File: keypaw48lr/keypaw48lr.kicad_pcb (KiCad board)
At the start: 2 copper layers, 0 parts

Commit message: feat: layout key matrix with kbplacer
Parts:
- added C1: 10uF, Capacitor_SMD:C_1206_3216Metric_Pad1.33x1.80mm_HandSolder, B.Cu at (97.8, 142.2)
- added C10: 1uF, Capacitor_SMD:C_1206_3216Metric_Pad1.33x1.80mm_HandSolder, B.Cu at (101.6, 150.6)
- added C11: 1uF, Capacitor_SMD:C_1206_3216Metric_Pad1.33x1.80mm_HandSolder, B.Cu at (60.4, 62.4)
- added C2: 100nF, Capacitor_SMD:C_0805_2012Metric_Pad1.18x1.45mm_HandSolder, B.Cu at (93.8, 142.2)
- added C3: 10uF, Capacitor_SMD:C_1206_3216Metric_Pad1.33x1.80mm_HandSolder, B.Cu at (91.2, 150.6)
- added C4: 100nF, Capacitor_SMD:C_0805_2012Metric_Pad1.18x1.45mm_HandSolder, B.Cu at (87.1, 150.6)
- added C5: 4.7uF, Capacitor_SMD:C_1206_3216Metric_Pad1.33x1.80mm_HandSolder, B.Cu at (112.6, 146.4)
- added C6: 100nF, Capacitor_SMD:C_0805_2012Metric_Pad1.18x1.45mm_HandSolder, B.Cu at (113.2, 143.0)
- added C7: 10uF, Capacitor_SMD:C_1206_3216Metric_Pad1.33x1.80mm_HandSolder, B.Cu at (125.2, 147.2)
- added C8: 100nF, Capacitor_SMD:C_0805_2012Metric_Pad1.18x1.45mm_HandSolder, B.Cu at (121.6, 147.2)
- added C9: 1uF, Capacitor_SMD:C_1206_3216Metric_Pad1.33x1.80mm_HandSolder, B.Cu at (111.4, 150.4)
- added D1: D, MX_SW_HS_REV:D_SOD-323_HandSoldering_REV, F.Cu at (83.6, 59.9)
- added D10: D, MX_SW_HS_REV:D_SOD-323_HandSoldering_REV, F.Cu at (140.7, 76.7)
- added D11: D, MX_SW_HS_REV:D_SOD-323_HandSoldering_REV, F.Cu at (159.8, 83.7)
- added D12: D, MX_SW_HS_REV:D_SOD-323_HandSoldering_REV, F.Cu at (178.8, 83.7)
- added D13: D, MX_SW_HS_REV:D_SOD-323_HandSoldering_REV, F.Cu at (83.6, 98.0)
- added D14: D, MX_SW_HS_REV:D_SOD-323_HandSoldering_REV, F.Cu at (102.6, 95.7)
- added D15: D, MX_SW_HS_REV:D_SOD-323_HandSoldering_REV, F.Cu at (121.7, 93.3)
- added D16: D, MX_SW_HS_REV:D_SOD-323_HandSoldering_REV, F.Cu at (140.7, 95.7)
- added D17: D, MX_SW_HS_REV:D_SOD-323_HandSoldering_REV, F.Cu at (159.8, 102.8)
- added D18: D, MX_SW_HS_REV:D_SOD-323_HandSoldering_REV, F.Cu at (178.8, 102.8)
- added D19: D, MX_SW_HS_REV:D_SOD-323_HandSoldering_REV, F.Cu at (76.4, 136.1)
- added D2: D, MX_SW_HS_REV:D_SOD-323_HandSoldering_REV, F.Cu at (102.6, 57.6)
- added D20: D, MX_SW_HS_REV:D_SOD-323_HandSoldering_REV, F.Cu at (64.5, 117.1)
- added D21: D, MX_SW_HS_REV:D_SOD-323_HandSoldering_REV, F.Cu at (83.6, 117.1)
- added D22: D, MX_SW_HS_REV:D_SOD-323_HandSoldering_REV, F.Cu at (87.2, 115.8)
- added D23: D, MX_SW_HS_REV:D_SOD-323_HandSoldering_REV, F.Cu at (159.8, 136.1)
- added D24: D, MX_SW_HS_REV:D_SOD-323_HandSoldering_REV, F.Cu at (178.8, 136.1)
- added D3: D, MX_SW_HS_REV:D_SOD-323_HandSoldering_REV, F.Cu at (121.7, 55.2)
- added D4: D, MX_SW_HS_REV:D_SOD-323_HandSoldering_REV, F.Cu at (140.7, 57.6)
- added D5: D, MX_SW_HS_REV:D_SOD-323_HandSoldering_REV, F.Cu at (159.8, 64.7)
- added D6: D, MX_SW_HS_REV:D_SOD-323_HandSoldering_REV, F.Cu at (178.8, 64.7)
- added D7: D, MX_SW_HS_REV:D_SOD-323_HandSoldering_REV, F.Cu at (83.6, 79.0)
- added D8: D, MX_SW_HS_REV:D_SOD-323_HandSoldering_REV, F.Cu at (102.6, 76.7)
- added D9: D, MX_SW_HS_REV:D_SOD-323_HandSoldering_REV, F.Cu at (121.7, 74.2)
- added J1: Conn_01x02, Connector_Molex:Molex_PicoBlade_53048-0210_1x02_P1.25mm_Horizontal, F.Cu at (105.4, 53.2)
- added J2: Conn_01x02, Connector_Molex:Molex_PicoBlade_53048-0210_1x02_P1.25mm_Horizontal, F.Cu at (65.2, 64.3)
- added J3: Conn_01x02, Connector_Molex:Molex_PicoBlade_53048-0210_1x02_P1.25mm_Horizontal, F.Cu at (94.4, 128.1)
- added J4: Conn_01x02, Connector_Molex:Molex_PicoBlade_53048-0210_1x02_P1.25mm_Horizontal, F.Cu at (170.0, 130.0)
- added J5: Conn_01x02, Connector_Molex:Molex_PicoBlade_53048-0210_1x02_P1.25mm_Horizontal, F.Cu at (177.6, 130.0)
- added J6: JD9613_OLED_FPC_Conn_01x10, JD9613_OLED_FPC:TE_1-1734839-0_1x10-1MP_P0.5mm_Horizontal, B.Cu at (56.2, 82.2)
- added J7: JD9613_OLED_FPC_Conn_01x10, JD9613_OLED_FPC:TE_1-1734839-0_1x10-1MP_P0.5mm_Horizontal, F.Cu at (56.3, 74.5)
- added JP1: SolderJumper_2_Open, Jumper:SolderJumper-2_P1.3mm_Open_TrianglePad1.0x1.5mm, B.Cu at (85.8, 55.3)
- added LED1: WS2812B, WS2812B_2020_V6:LED_WS2812B-2020_backmount_rev, F.Cu at (76.2, 56.9)
- added LED10: WS2812B, WS2812B_2020_V6:LED_WS2812B-2020_backmount_rev, F.Cu at (133.3, 73.7)
- added LED11: WS2812B, WS2812B_2020_V6:LED_WS2812B-2020_backmount_rev, F.Cu at (152.4, 80.7)
- added LED12: WS2812B, WS2812B_2020_V6:LED_WS2812B-2020_backmount_rev, F.Cu at (171.4, 80.7)
- added LED13: WS2812B, WS2812B_2020_V6:LED_WS2812B-2020_backmount_rev, F.Cu at (76.2, 95.0)
- added LED14: WS2812B, WS2812B_2020_V6:LED_WS2812B-2020_backmount_rev, F.Cu at (95.2, 92.7)
- added LED15: WS2812B, WS2812B_2020_V6:LED_WS2812B-2020_backmount_rev, F.Cu at (114.3, 90.2)
- added LED16: WS2812B, WS2812B_2020_V6:LED_WS2812B-2020_backmount_rev, F.Cu at (133.3, 92.7)
- added LED17: WS2812B, WS2812B_2020_V6:LED_WS2812B-2020_backmount_rev, F.Cu at (152.4, 99.8)
- added LED18: WS2812B, WS2812B_2020_V6:LED_WS2812B-2020_backmount_rev, F.Cu at (171.4, 99.8)
- added LED19: WS2812B, WS2812B_2020_V6:LED_WS2812B-2020_backmount_rev, F.Cu at (69.1, 133.1)
- added LED2: WS2812B, WS2812B_2020_V6:LED_WS2812B-2020_backmount_rev, F.Cu at (95.2, 54.6)
- added LED20: WS2812B, WS2812B_2020_V6:LED_WS2812B-2020_backmount_rev, F.Cu at (57.1, 114.1)
- added LED21: WS2812B, WS2812B_2020_V6:LED_WS2812B-2020_backmount_rev, F.Cu at (76.2, 114.1)
- added LED22: WS2812B, WS2812B_2020_V6:LED_WS2812B-2020_backmount_rev, F.Cu at (95.2, 111.8)
- added LED23: WS2812B, WS2812B_2020_V6:LED_WS2812B-2020_backmount_rev, F.Cu at (152.4, 133.1)
- added LED24: WS2812B, WS2812B_2020_V6:LED_WS2812B-2020_backmount_rev, F.Cu at (171.4, 133.1)
- added LED3: WS2812B, WS2812B_2020_V6:LED_WS2812B-2020_backmount_rev, F.Cu at (114.3, 52.1)
- added LED4: WS2812B, WS2812B_2020_V6:LED_WS2812B-2020_backmount_rev, F.Cu at (133.3, 54.6)
- added LED5: WS2812B, WS2812B_2020_V6:LED_WS2812B-2020_backmount_rev, F.Cu at (152.4, 61.7)
- added LED6: WS2812B, WS2812B_2020_V6:LED_WS2812B-2020_backmount_rev, F.Cu at (171.4, 61.7)
- added LED7: WS2812B, WS2812B_2020_V6:LED_WS2812B-2020_backmount_rev, F.Cu at (76.2, 76.0)
- added LED8: WS2812B, WS2812B_2020_V6:LED_WS2812B-2020_backmount_rev, F.Cu at (95.2, 73.7)
- added LED9: WS2812B, WS2812B_2020_V6:LED_WS2812B-2020_backmount_rev, F.Cu at (114.3, 71.2)
- added MX1: MX_SW_HS, MX_SW_HS_REV:SW_MX_HS_REV, F.Cu at (76.2, 61.9)
- added MX10: MX_SW_HS, MX_SW_HS_REV:SW_MX_HS_REV, F.Cu at (133.3, 78.7)
- added MX11: MX_SW_HS, MX_SW_HS_REV:SW_MX_HS_REV, F.Cu at (152.4, 85.7)
- added MX12: MX_SW_HS, MX_SW_HS_REV:SW_MX_HS_REV, F.Cu at (171.4, 85.7)
- added MX13: MX_SW_HS, MX_SW_HS_REV:SW_MX_HS_REV, F.Cu at (76.2, 100.0)
- added MX14: MX_SW_HS, MX_SW_HS_REV:SW_MX_HS_REV, F.Cu at (95.2, 97.7)
- added MX15: MX_SW_HS, MX_SW_HS_REV:SW_MX_HS_REV, F.Cu at (114.3, 95.2)
- added MX16: MX_SW_HS, MX_SW_HS_REV:SW_MX_HS_REV, F.Cu at (133.3, 97.7)
- added MX17: MX_SW_HS, MX_SW_HS_REV:SW_MX_HS_REV, F.Cu at (152.4, 104.8)
- added MX18: MX_SW_HS, MX_SW_HS_REV:SW_MX_HS_REV, F.Cu at (171.4, 104.8)
- added MX19: MX_SW_HS, MX_SW_HS_REV:SW_MX_HS_REV, F.Cu at (69.1, 138.1)
- added MX2: MX_SW_HS, MX_SW_HS_REV:SW_MX_HS_REV, F.Cu at (95.2, 59.6)
- added MX20: MX_SW_HS, MX_SW_HS_REV:SW_MX_HS_REV, F.Cu at (57.1, 119.1)
- added MX21: MX_SW_HS, MX_SW_HS_REV:SW_MX_HS_REV, F.Cu at (76.2, 119.1)
- added MX22: MX_SW_HS, MX_SW_HS_REV:SW_MX_HS_REV, B.Cu at (95.2, 116.8)
- added MX23: MX_SW_HS, MX_SW_HS_REV:SW_MX_HS_REV, F.Cu at (152.4, 138.1)
- added MX24: MX_SW_HS, MX_SW_HS_REV:SW_MX_HS_REV, F.Cu at (171.4, 138.1)
- added MX3: MX_SW_HS, MX_SW_HS_REV:SW_MX_HS_REV, F.Cu at (114.3, 57.1)
- added MX4: MX_SW_HS, MX_SW_HS_REV:SW_MX_HS_REV, F.Cu at (133.3, 59.6)
- added MX5: MX_SW_HS, MX_SW_HS_REV:SW_MX_HS_REV, F.Cu at (152.4, 66.7)
- added MX6: MX_SW_HS, MX_SW_HS_REV:SW_MX_HS_REV, F.Cu at (171.4, 66.7)
- added MX7: MX_SW_HS, MX_SW_HS_REV:SW_MX_HS_REV, F.Cu at (76.2, 81.0)
- added MX8: MX_SW_HS, MX_SW_HS_REV:SW_MX_HS_REV, F.Cu at (95.2, 78.7)
- added MX9: MX_SW_HS, MX_SW_HS_REV:SW_MX_HS_REV, F.Cu at (114.3, 76.2)
- added R1: 2M, Resistor_SMD:R_1206_3216Metric_Pad1.30x1.75mm_HandSolder, B.Cu at (54.4, 68.6)
- added R2: 2M, Resistor_SMD:R_1206_3216Metric_Pad1.30x1.75mm_HandSolder, B.Cu at (54.8, 89.2)
- added R3: 5.6R, Resistor_SMD:R_1206_3216Metric_Pad1.30x1.75mm_HandSolder, B.Cu at (127.3, 128.2)
- added R4: 10k, Resistor_SMD:R_1206_3216Metric_Pad1.30x1.75mm_HandSolder, B.Cu at (127.3, 131.5)
- added R5: 100k, Resistor_SMD:R_1206_3216Metric_Pad1.30x1.75mm_HandSolder, B.Cu at (149.2, 119.5)
- added R6: 100k, Resistor_SMD:R_1206_3216Metric_Pad1.30x1.75mm_HandSolder, B.Cu at (149.2, 122.8)
- added SW1: SW_SPDT, Button_Switch_SMD:SW_SPDT_CK_JS102011SAQN, B.Cu at (72.3, 44.6)
- added SW2: RotaryEncoder, ALPS_EC10E:RotaryEncoder_Alps_EC10E-Switch, F.Cu at (156.9, 121.2)
- added U1: nice_nano, PCM_marbastlib-xp-promicroish:nice_nano_AH_USBup, F.Cu at (56.2, 84.4)
- added U2: PAW3395, paw3395_pcb:PAW3395, F.Cu at (107.0, 137.7)
- added U3: TLV70019_SOT23-5, Package_TO_SOT_SMD:SOT-23-5_HandSoldering, B.Cu at (106.4, 150.6)
- added U4: TPS22917DBV, Package_TO_SOT_SMD:SOT-23-6_Handsoldering, B.Cu at (55.0, 62.8)
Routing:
- net COL5: track 0.00 -> 18.9 mm
- net COL3: track 0.00 -> 18.9 mm
- net COL0: track 0.00 -> 18.9 mm
- net COL1: track 0.00 -> 18.9 mm
- net COL2: track 0.00 -> 18.9 mm
- net COL4: track 0.00 -> 18.9 mm
- net Net-(D17-A): track 0.00 -> 8.16 mm
- net Net-(D11-A): track 0.00 -> 8.16 mm
- net Net-(D19-A): track 0.00 -> 8.16 mm
- net Net-(D9-A): track 0.00 -> 8.16 mm
- net Net-(D8-A): track 0.00 -> 8.16 mm
- net Net-(D7-A): track 0.00 -> 8.16 mm
- net Net-(D23-A): track 0.00 -> 8.16 mm
- net Net-(D14-A): track 0.00 -> 8.16 mm
- net Net-(D13-A): track 0.00 -> 8.16 mm
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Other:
- board outline added: 155 x 115 mm

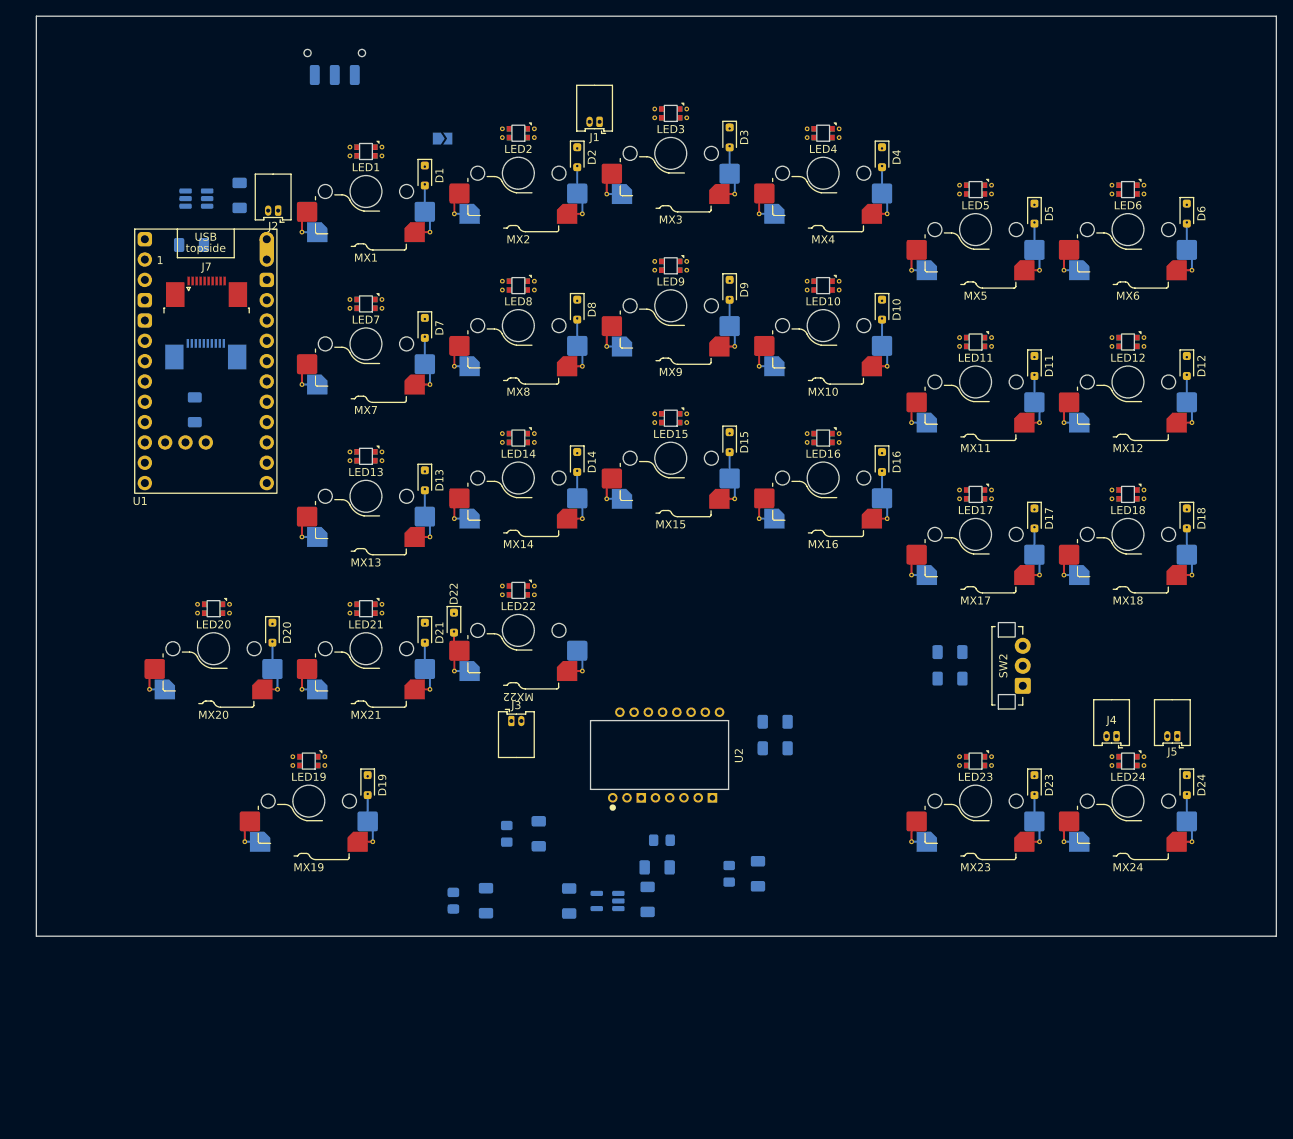
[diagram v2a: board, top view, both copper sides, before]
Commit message: feat: multichannel wiring the leds
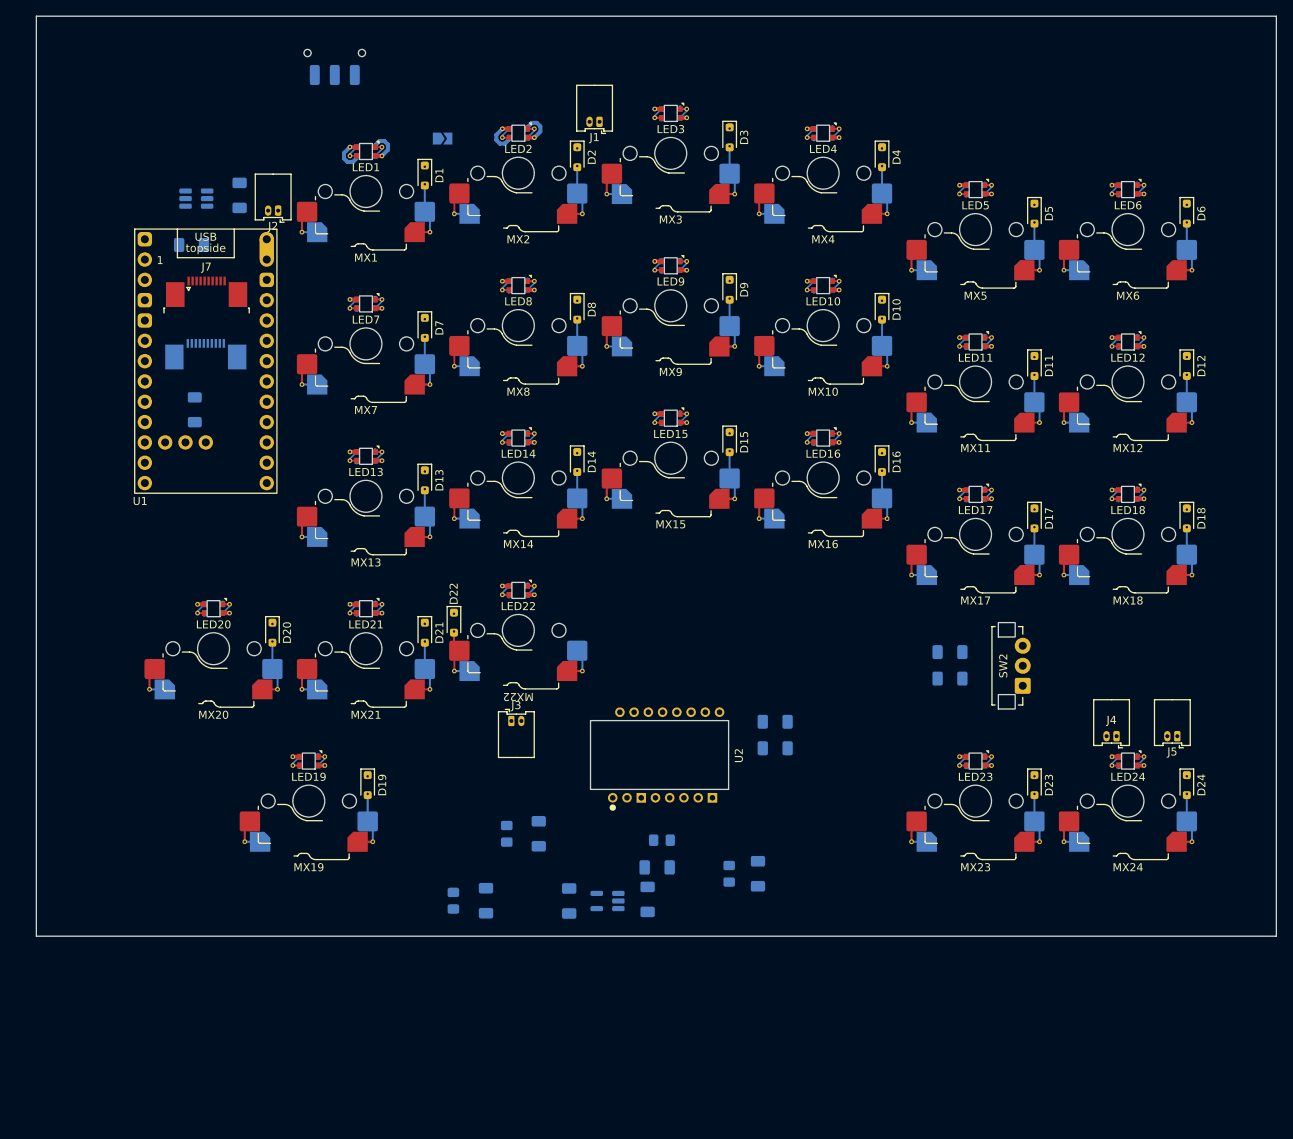
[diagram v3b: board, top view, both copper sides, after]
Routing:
- net V_peri: track 0.00 -> 33.0 mm
- net GND: track 0.00 -> 32.9 mm
- net Net-(LED17-DOUT): track 0.00 -> 4.60 mm
- net Net-(LED11-DOUT): track 0.00 -> 4.60 mm
- net Net-(LED5-DOUT): track 0.00 -> 4.60 mm
- net Net-(LED23-DOUT): track 0.00 -> 4.60 mm
- net Net-(LED7-DOUT): track 0.00 -> 4.60 mm
- net Net-(LED19-DOUT): track 0.00 -> 4.60 mm
- net Net-(LED8-DOUT): track 0.00 -> 4.60 mm
- net Net-(LED2-DOUT): track 0.00 -> 4.60 mm
- net Net-(LED1-DOUT): track 0.00 -> 4.60 mm
- net Net-(LED21-DOUT): track 0.00 -> 4.60 mm
- net Net-(LED14-DOUT): track 0.00 -> 4.60 mm
- net Net-(LED13-DOUT): track 0.00 -> 4.60 mm
- net Net-(LED10-DOUT): track 0.00 -> 4.60 mm
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
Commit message: feat: basic key matrix wiring
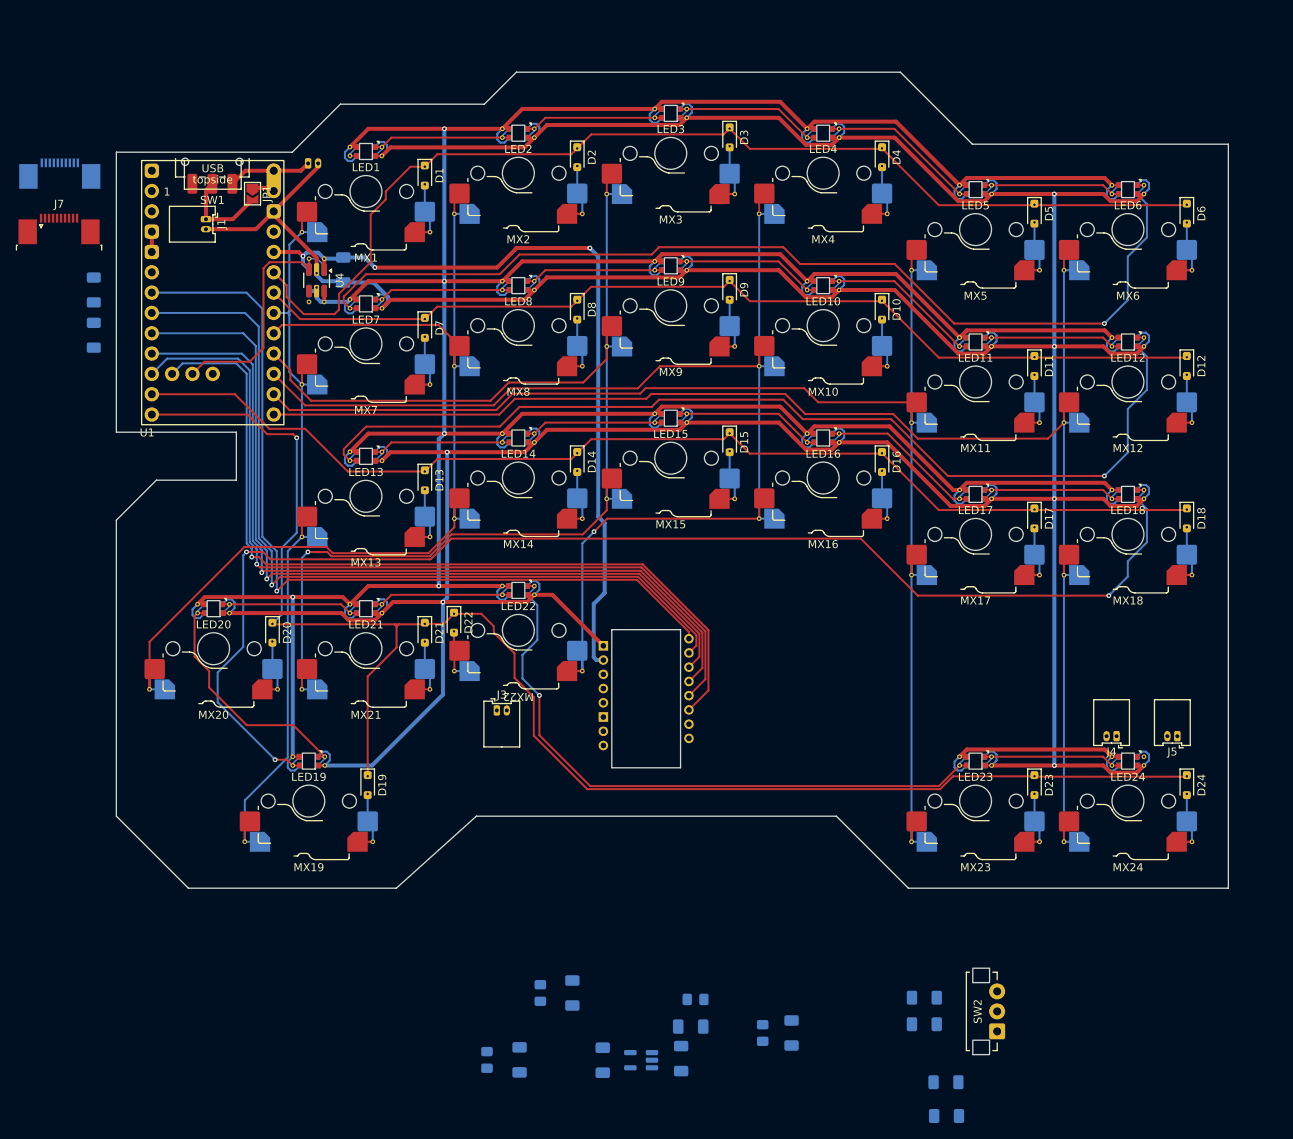
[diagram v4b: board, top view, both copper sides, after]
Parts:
- J2, U2: moved to B.Cu
- JP1, SW1: moved to F.Cu
- U4: footprint Package_TO_SOT_SMD:SOT-23-6_Handsoldering -> MX_SW_HS_REV:SOT-23-6_Handsoldering_REV; moved to F.Cu
- moved R4 50.7 mm to (148.8, 177.5)
- moved J1 50.7 mm to (56.2, 65.4), turned to -90 degrees
- moved R3 49.9 mm to (148.7, 173.2)
- moved R5 43.3 mm to (146.0, 162.7)
- moved R6 43.3 mm to (146.0, 166.0)
- moved SW2 43.3 mm to (153.7, 164.4)
- moved J6 29.0 mm to (37.9, 59.7)
- moved JP1 24.7 mm to (62.0, 62.2), turned to -90 degrees
- moved SW1 20.5 mm to (57.0, 58.2), turned to 180 degrees
- moved C1 20.3 mm to (102.0, 162.1)
- moved C10 20.3 mm to (105.8, 170.5)
- moved C2 20.3 mm to (98.0, 162.1)
- moved C3 20.3 mm to (95.4, 170.5)
- moved C4 20.3 mm to (91.3, 170.5)
- moved C5 20.3 mm to (116.8, 166.3)
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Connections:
- J1 pad 1: Net-(J1-Pin_1) -> /BATT_J1+
- JP1 pad 2: Net-(J1-Pin_1) -> /BATT_J1+
- LED13 pad 3: Net-(LED13-DIN) -> Net-(LED12-DOUT)
- LED19 pad 3: unconnected-(LED19-DIN-Pad3) -> Net-(LED18-DOUT)
- LED24 pad 1: Net-(LED18-DOUT) -> unconnected-(LED24-DOUT-Pad1)
- LED6 pad 1: Net-(LED12-DOUT) -> Net-(LED6-DOUT)
- LED7 pad 3: Net-(LED13-DIN) -> Net-(LED6-DOUT)
- R1 pad 1: GND -> +3.3V
- R1 pad 2: PERI_EN -> NRESET
- R2 pad 1: +3.3V -> GND
- R2 pad 2: NRESET -> PERI_EN
- SW1 pad 1: unconnected-(SW1-A-Pad1) -> +BATT
- SW1 pad 2: +BATT -> /BATT_J1+
- SW1 pad 3: Net-(J1-Pin_1) -> unconnected-(SW1-C-Pad3)
- U1 pad 10: DS_OLED -> CS_PAW
- U1 pad 11: ROW3 -> ROW2
- U1 pad 12: ROW2 -> ROW3
- U1 pad 2: SCK -> DS_OLED
- U1 pad 25: PERI_EN -> NRESET
- U1 pad 26: NRESET -> PERI_EN
- U1 pad 5: SDO -> CS_OLED
- U1 pad 6: SDI -> MOTION
- U1 pad 7: CS_PAW -> SCK
- U1 pad 8: MOTION -> SDO
- U1 pad 9: CS_OLED -> SDI
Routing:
- net GND: track 32.9 -> 648.8 mm, vias 0 -> 6
- net V_peri: track 33.0 -> 560.4 mm, vias 0 -> 5
- net ROW3: track 0.00 -> 194.6 mm, vias 0 -> 1
- net COL5: track 18.9 -> 193.3 mm
- net Net-(LED18-DOUT): track 4.60 -> 164.3 mm, vias 0 -> 3
- net COL4: track 18.9 -> 173.3 mm
- net COL2: track 18.9 -> 164.3 mm, vias 0 -> 1
- net COL3: track 18.9 -> 160.6 mm, vias 0 -> 1
- net ROW2: track 0.00 -> 139.4 mm
- net ROW0: track 0.00 -> 136.1 mm
- net Net-(LED6-DOUT): track 0.00 -> 126.9 mm, vias 0 -> 1
- net Net-(LED12-DOUT): track 4.60 -> 126.9 mm, vias 0 -> 1
- net ROW1: track 0.00 -> 121.6 mm
- net COL1: track 18.9 -> 133.4 mm
- net CS_PAW: track 0.00 -> 106.7 mm, vias 0 -> 1
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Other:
- board size 155 x 115 mm -> 139 x 102 mm

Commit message: feat: finish pcb wiring draft
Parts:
- J3, J4, J5, SW2: moved to B.Cu
- R1, R2, R5, R6: moved to F.Cu
- moved R4 61.7 mm to (141.5, 116.2), turned to 0 degrees
- moved C7 59.2 mm to (106.3, 112.6), turned to 0 degrees
- moved C8 55.8 mm to (105.7, 115.1), turned to 0 degrees
- moved R3 52.5 mm to (118.8, 130.1), turned to 90 degrees
- moved C4 48.0 mm to (121.1, 132.7)
- moved C3 46.6 mm to (123.5, 133.3)
- moved C5 46.3 mm to (92.9, 126.6), turned to -90 degrees
- moved C6 45.7 mm to (90.4, 126.0), turned to -90 degrees
- moved U3 45.7 mm to (100.9, 125.9)
- moved C9 42.3 mm to (102.1, 130.2)
- moved C10 40.8 mm to (99.7, 130.2)
- moved R5 40.6 mm to (153.2, 122.7), turned to 0 degrees
- moved SW2 39.8 mm to (146.9, 125.2), turned to -90 degrees
- moved R6 39.1 mm to (153.2, 127.6), turned to 0 degrees
- moved C2 32.6 mm to (95.0, 129.6)
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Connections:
- net Net-(U2-VDDREG) renamed /PAW_VDD
- J3 pad 1: Net-(D22-A) -> COL3
- J3 pad 2: COL3 -> Net-(D22-A)
- J4 pad 1: Net-(D23-A) -> COL4
- J4 pad 2: COL4 -> Net-(D23-A)
- J5 pad 1: Net-(D24-A) -> COL5
- J5 pad 2: COL5 -> Net-(D24-A)
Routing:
- net GND: track 648.8 -> 761.0 mm, vias 6 -> 7
- net +3.3V: track 99.0 -> 191.2 mm, vias 3 -> 4
- net V_peri: track 560.4 -> 639.4 mm, vias 5 -> 9
- net MOTION: track 106.4 -> 154.8 mm, vias 1 -> 2
- net +1V9: track 0.00 -> 44.3 mm, vias 0 -> 3
- net CS_PAW: track 106.7 -> 142.2 mm, vias 1 -> 3
- net CS_OLED: track 0.00 -> 29.6 mm, vias 0 -> 1
- net Net-(D23-A): track 8.16 -> 35.9 mm
- net NRESET: track 105.4 -> 133.0 mm, vias 1 -> 2
- net SDI: track 104.8 -> 132.2 mm
- net LED: track 2.30 -> 29.0 mm
- net COL4: track 173.3 -> 198.1 mm, vias 0 -> 1
- net SDO: track 105.5 -> 128.0 mm, vias 1 -> 2
- net COL3: track 160.6 -> 179.2 mm
- net DS_OLED: track 0.00 -> 18.0 mm, vias 0 -> 1
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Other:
- outline, holes or cut-outs redrawn
